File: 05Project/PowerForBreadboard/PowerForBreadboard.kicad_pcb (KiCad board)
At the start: 2 copper layers, 33.1 x 55.9 mm, 16 parts, among them J1 Barrel_Jack_Switch, J2 Power2, J3 Power1, U1 L7805

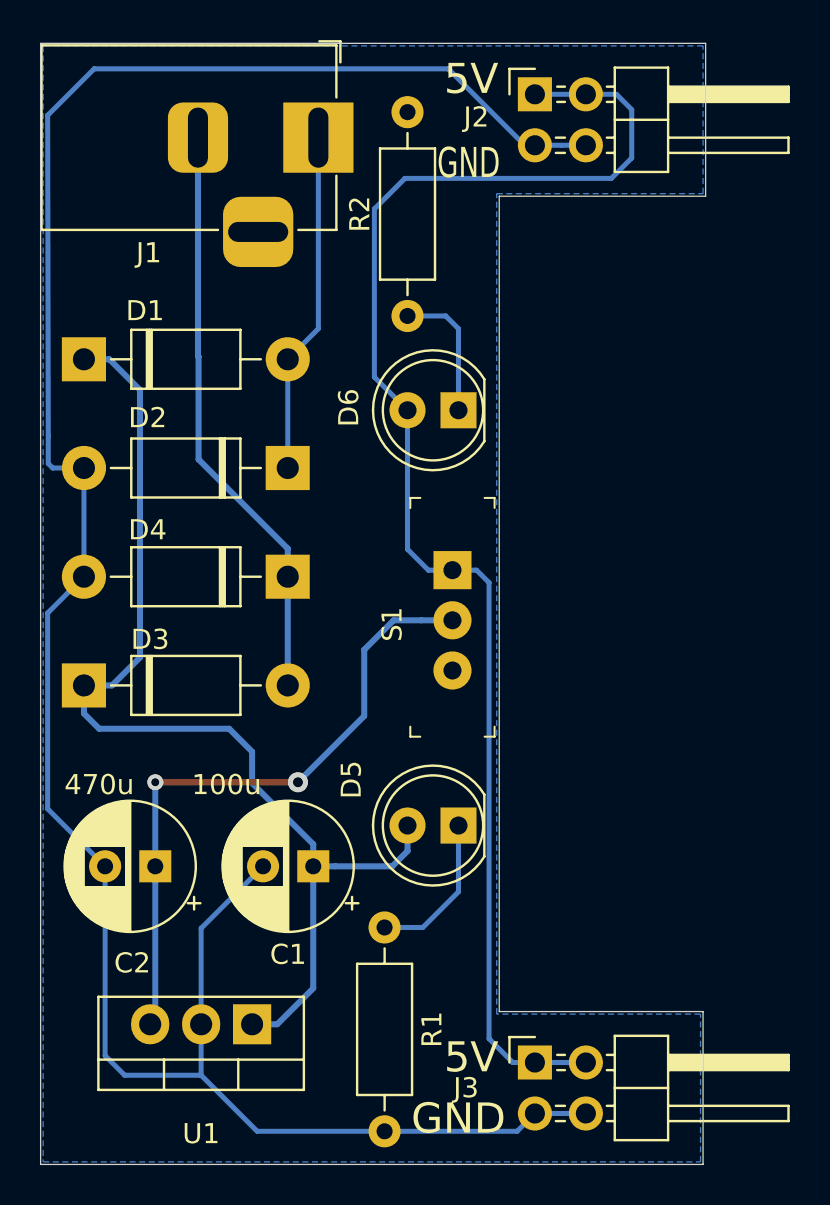
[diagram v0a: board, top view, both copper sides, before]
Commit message: Update rounded corner
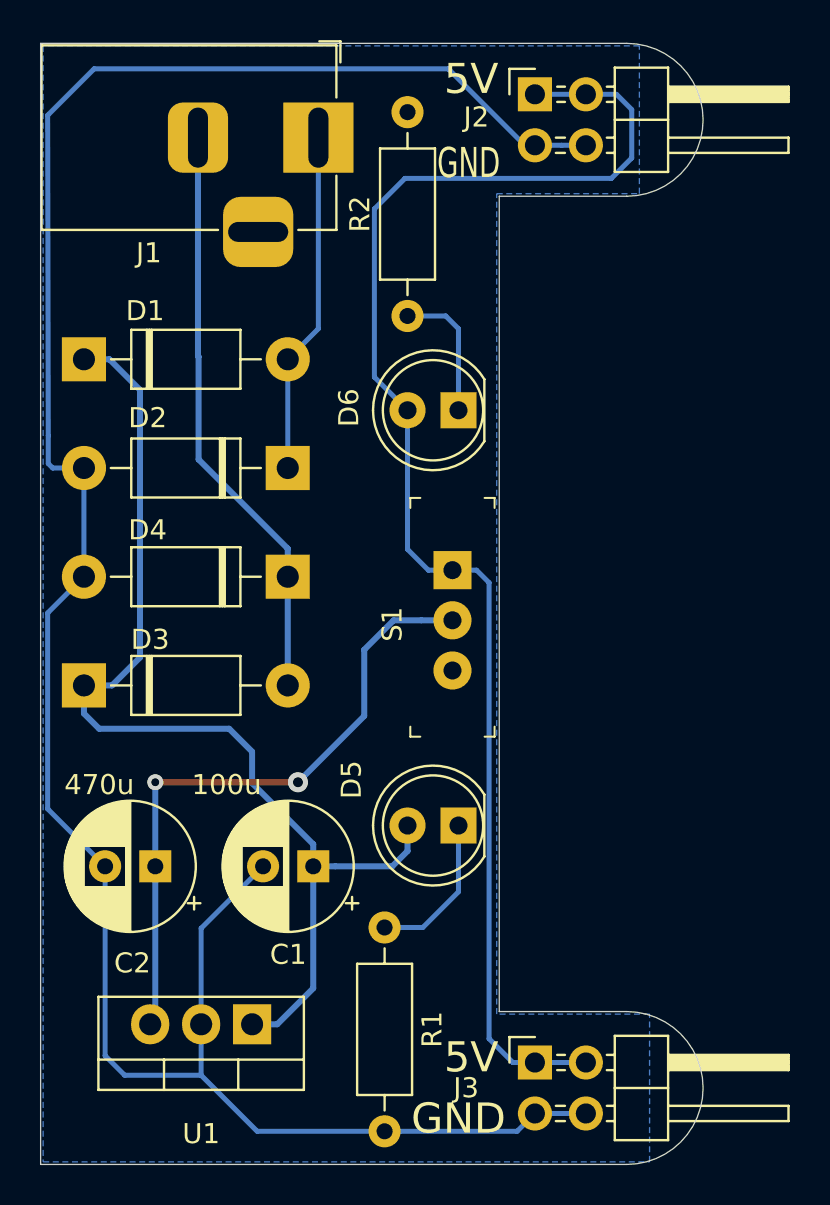
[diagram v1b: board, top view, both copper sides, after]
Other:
- board size 33.1 x 55.9 mm -> 33 x 55.9 mm
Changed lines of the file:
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@@
   (page A4)
   (layers
-    (0 F.Cu signal)
+    (0 F.Cu signal hide)
     (31 B.Cu signal)
-    (32 B.Adhes user)
-    (33 F.Adhes user)
-    (34 B.Paste user)
-    (35 F.Paste user)
-    (36 B.SilkS user)
-    (37 F.SilkS user)
-    (38 B.Mask user)
-    (39 F.Mask user)
-    (40 Dwgs.User user)
-    (41 Cmts.User user)
-    (42 Eco1.User user)
-    (43 Eco2.User user)
+    (32 B.Adhes user hide)
+    (33 F.Adhes user hide)
+    (34 B.Paste user hide)
+    (35 F.Paste user hide)
+    (36 B.SilkS user hide)
+    (37 F.SilkS user hide)
+    (38 B.Mask user hide)
+    (39 F.Mask user hide)
+    (40 Dwgs.User user hide)
+    (41 Cmts.User user hide)
+    (42 Eco1.User user hide)
+    (43 Eco2.User user hide)
     (44 Edge.Cuts user)
-    (45 Margin user)
-    (46 B.CrtYd user)
-    (47 F.CrtYd user)
-    (48 B.Fab user)
-    (49 F.Fab user)
+    (45 Margin user hide)
+    (46 B.CrtYd user hide)
+    (47 F.CrtYd user hide)
+    (48 B.Fab user hide)
+    (49 F.Fab user hide)
   )
   (setup
@@
     (pcbplotparams
       (layerselection 0x010fc_ffffffff)
-      (usegerberextensions false)
+      (usegerberextensions true)
       (usegerberattributes false)
       (usegerberadvancedattributes false)
@@
       (outputformat 1)
       (mirror false)
-      (drillshape 1)
+      (drillshape 0)
       (scaleselection 1)
-      (outputdirectory ""))
+      (outputdirectory "gerbers/"))
   )
   (net 0 "")
@@
     )
   )
+  (gr_arc (start 162.56 119.38) (end 162.56 123.19) (angle -180) (layer Edge.Cuts) (width 0.05))
+  (gr_arc (start 162.56 71.12) (end 162.56 74.93) (angle -180) (layer Edge.Cuts) (width 0.05))
   (gr_text "Luan Pham\nTechMaker.vn" (at 149.098 87.122 90) (layer B.SilkS)
     (effects (font (size 1.5 1.5) (thickness 0.3)) (justify left mirror))
@@
     (effects (font (size 1.5 1.5) (thickness 0.3)))
   )
-  (gr_line (start 133.35 67.31) (end 166.497 67.31) (layer Edge.Cuts) (width 0.05))
-  (gr_line (start 166.497 74.93) (end 166.497 67.31) (layer Edge.Cuts) (width 0.05))
-  (gr_line (start 156.21 74.93) (end 166.497 74.93) (layer Edge.Cuts) (width 0.05))
+  (gr_line (start 133.35 67.31) (end 162.56 67.31) (layer Edge.Cuts) (width 0.05))
+  (gr_line (start 156.21 74.93) (end 162.56 74.93) (layer Edge.Cuts) (width 0.05))
   (gr_line (start 156.21 115.57) (end 156.21 74.93) (layer Edge.Cuts) (width 0.05))
-  (gr_line (start 166.37 115.57) (end 156.21 115.57) (layer Edge.Cuts) (width 0.05))
-  (gr_line (start 166.37 123.19) (end 166.37 115.57) (layer Edge.Cuts) (width 0.05))
-  (gr_line (start 133.35 123.19) (end 166.37 123.19) (layer Edge.Cuts) (width 0.05))
+  (gr_line (start 162.56 115.57) (end 156.21 115.57) (layer Edge.Cuts) (width 0.05))
+  (gr_line (start 133.35 123.19) (end 162.56 123.19) (layer Edge.Cuts) (width 0.05))
   (gr_line (start 133.35 67.31) (end 133.35 123.19) (layer Edge.Cuts) (width 0.05))
   (segment (start 159.325919 72.39) (end 157.988 72.39) (width 0.25) (layer B.Cu) (net 1))
@@
     (polygon
       (pts
-        (xy 133.477 67.437) (xy 133.477 123.063) (xy 166.243 123.063) (xy 166.243 115.697) (xy 156.083 115.697)
-        (xy 156.083 74.803) (xy 166.37 74.803) (xy 166.37 67.437)
+        (xy 133.477 67.437) (xy 133.477 123.063) (xy 163.703 123.063) (xy 163.703 115.697) (xy 156.083 115.697)
+        (xy 156.083 74.803) (xy 163.195 74.803) (xy 163.195 67.437)
       )
     )
